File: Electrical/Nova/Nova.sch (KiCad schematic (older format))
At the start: 15 parts, among them J2 Conn_02x04_Counter_Clockwise, U1 STM32F411CEUx

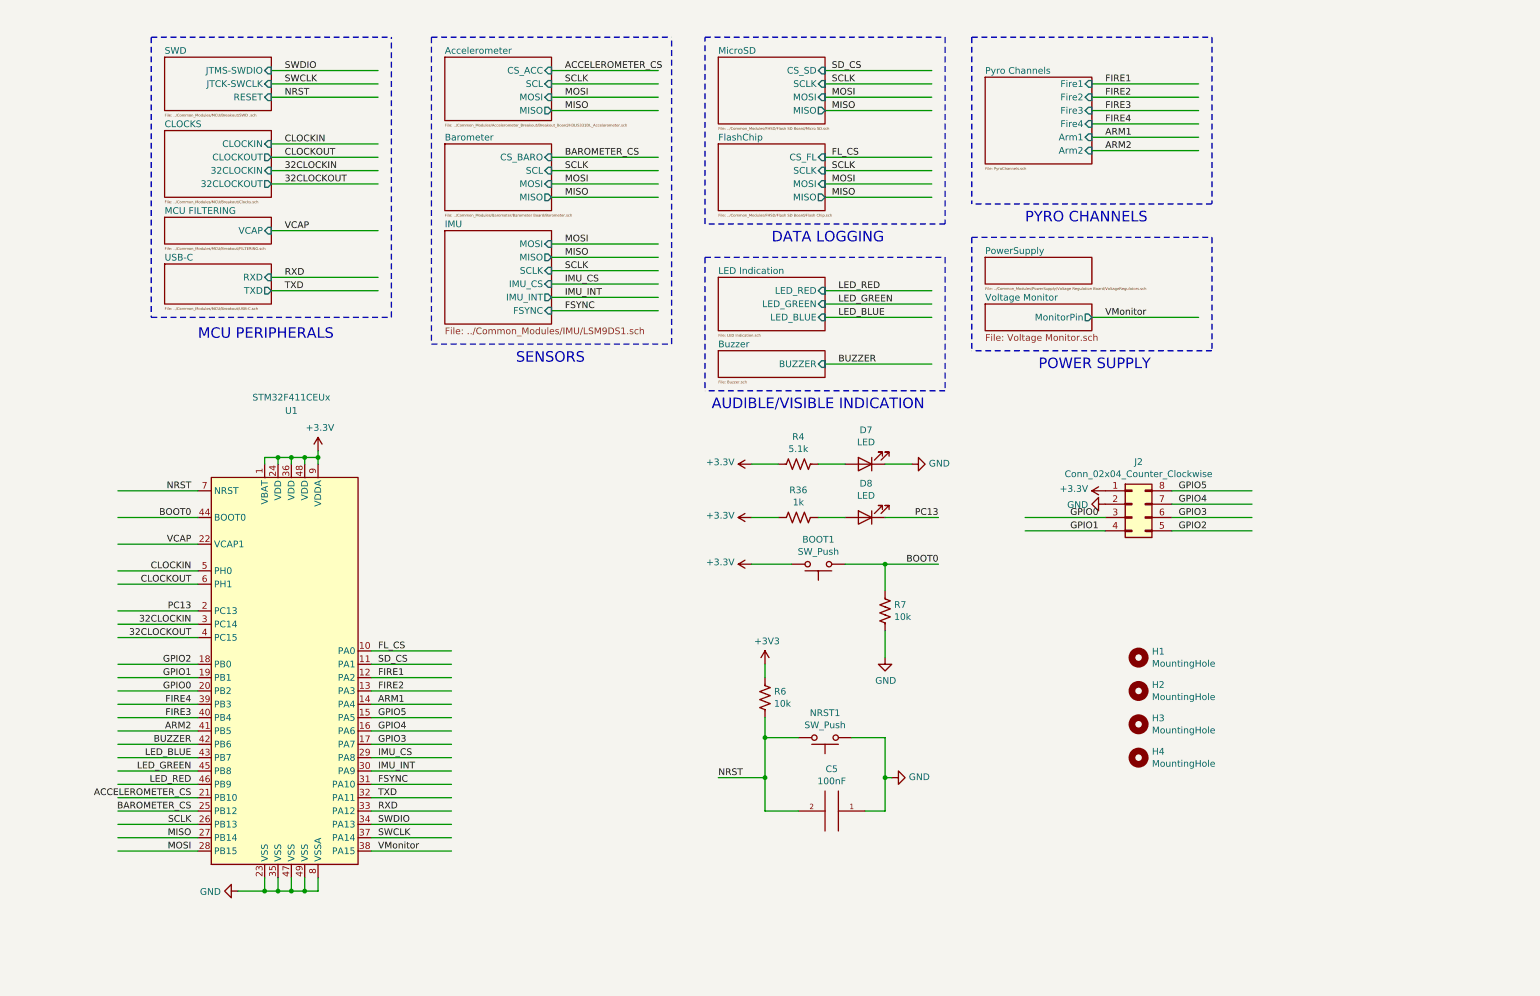
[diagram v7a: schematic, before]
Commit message: Flipped SD, fixed U8 pads, & put 2 INT pins on Accelerometer
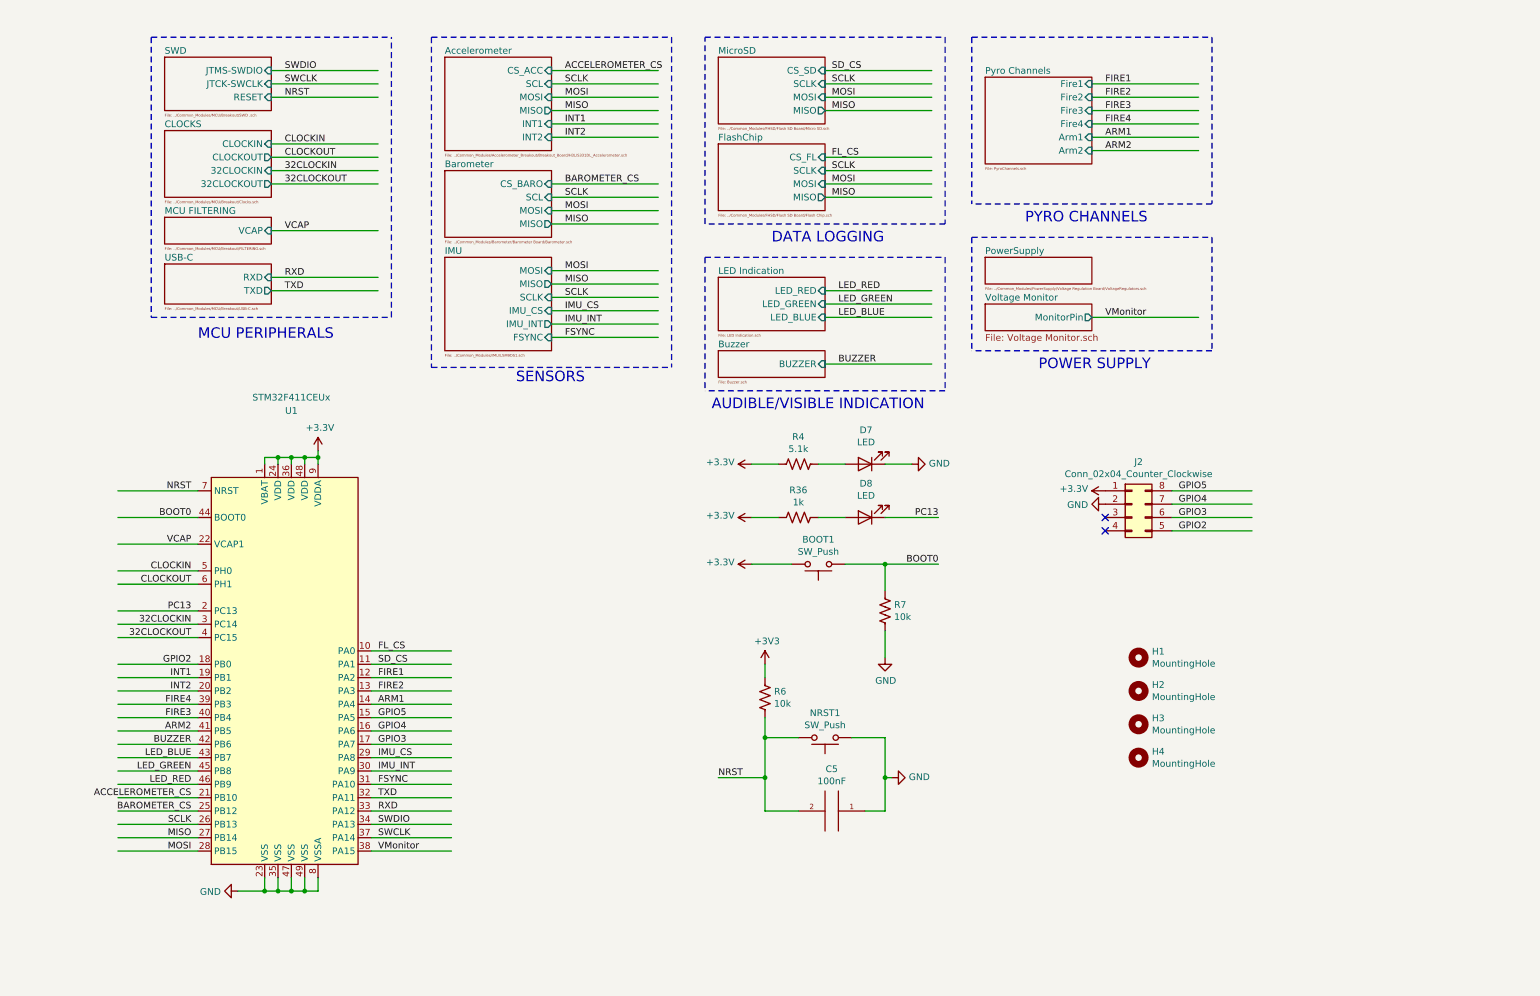
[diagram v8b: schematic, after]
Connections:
- net labels added: INT1, INT2
- net labels removed: GPIO0, GPIO1
- no-connect marks 0 -> 2
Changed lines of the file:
@@
 Wire Wire Line
 	6600 2850 7400 2850
-Text Notes 4800 3329 2    79   ~ 0
+Text Notes 4800 3475 2    79   ~ 0
 SENSORS\n\n
 Text Label 6650 1100 0    50   ~ 0
@@
 	5350 1100 4550 1100
 $Sheet
-S 3750 900  800  475
+S 3750 900  800  700
 U 5F46051D
 F0 "Accelerometer" 50
@@
 F4 "MISO" O R 4550 1300 50
 F5 "MOSI" I R 4550 1200 50
+F6 "INT1" I R 4550 1400 50
+F7 "INT2" I R 4550 1500 50
 $EndSheet
 Text Label 4650 1100 0    50   ~ 0
@@
 	5350 1200 4550 1200
 $Sheet
-S 3750 1550 800  500
+S 3750 1750 800  500
 U 5F3A063C
 F0 "Barometer" 50
 F1 "../Common_Modules/Barometer/Barometer Board/Barometer.sch" 20
-F2 "SCL" I R 4550 1750 50
-F3 "MOSI" I R 4550 1850 50
-F4 "MISO" O R 4550 1950 50
-F5 "CS_BARO" I R 4550 1650 50
+F2 "SCL" I R 4550 1950 50
+F3 "MOSI" I R 4550 2050 50
+F4 "MISO" O R 4550 2150 50
+F5 "CS_BARO" I R 4550 1850 50
 $EndSheet
-Text Label 4650 1750 0    50   ~ 0
+Text Label 4650 1950 0    50   ~ 0
 SCLK
-Text Label 4650 1950 0    50   ~ 0
+Text Label 4650 2150 0    50   ~ 0
 MISO
-Text Label 4650 1850 0    50   ~ 0
+Text Label 4650 2050 0    50   ~ 0
 MOSI
 Wire Wire Line
-	4550 1650 5350 1650
+	4550 1850 5350 1850
+Wire Wire Line
+	5350 2150 4550 2150
+Wire Wire Line
+	5350 2050 4550 2050
 Wire Wire Line
 	5350 1950 4550 1950
-Wire Wire Line
-	5350 1850 4550 1850
-Wire Wire Line
-	5350 1750 4550 1750
 Wire Wire Line
 	7400 1100 6600 1100
@@
 FL_CS
 Wire Notes Line
-	3650 3050 5450 3050
+	3650 3225 5450 3225
 Wire Notes Line
 	3650 750  5450 750
@@
 Text Label 3250 6650 0    50   ~ 0
 SWDIO
-Text Label 4650 1650 0    50   ~ 0
+Text Label 4650 1850 0    50   ~ 0
 BAROMETER_CS
 Text Label 4650 1000 0    50   ~ 0
@@
 	6150 5450 6150 5550
 $Sheet
-S 3750 2200 800  700
+S 3750 2400 800  700
 U 6029A10C
 F0 "IMU" 50
-F1 "../Common_Modules/IMU/LSM9DS1.sch" 50
-F2 "MOSI" I R 4550 2300 50
-F3 "MISO" O R 4550 2400 50
-F4 "SCLK" I R 4550 2500 50
-F5 "IMU_CS" I R 4550 2600 50
-F6 "IMU_INT" O R 4550 2700 50
-F7 "FSYNC" I R 4550 2800 50
+F1 "../Common_Modules/IMU/LSM9DS1.sch" 20
+F2 "MOSI" I R 4550 2500 50
+F3 "MISO" O R 4550 2600 50
+F4 "SCLK" I R 4550 2700 50
+F5 "IMU_CS" I R 4550 2800 50
+F6 "IMU_INT" O R 4550 2900 50
+F7 "FSYNC" I R 4550 3000 50
 $EndSheet
 Wire Wire Line
-	4550 2300 5350 2300
+	4550 2500 5350 2500
+Wire Wire Line
+	5350 2800 4550 2800
+Wire Wire Line
+	5350 2700 4550 2700
 Wire Wire Line
 	5350 2600 4550 2600
 Wire Wire Line
-	5350 2500 4550 2500
-Wire Wire Line
-	5350 2400 4550 2400
-Wire Wire Line
-	5350 2800 4550 2800
-Wire Wire Line
-	5350 2700 4550 2700
-Text Label 4650 2300 0    50   ~ 0
+	5350 3000 4550 3000
+Wire Wire Line
+	5350 2900 4550 2900
+Text Label 4650 2500 0    50   ~ 0
 MOSI
-Text Label 4650 2400 0    50   ~ 0
+Text Label 4650 2600 0    50   ~ 0
 MISO
-Text Label 4650 2500 0    50   ~ 0
+Text Label 4650 2700 0    50   ~ 0
 SCLK
-Text Label 4650 2600 0    50   ~ 0
+Text Label 4650 2800 0    50   ~ 0
 IMU_CS
-Text Label 4650 2700 0    50   ~ 0
+Text Label 4650 2900 0    50   ~ 0
 IMU_INT
-Text Label 4650 2800 0    50   ~ 0
+Text Label 4650 3000 0    50   ~ 0
 FSYNC
-Wire Notes Line
-	5450 3050 5450 750
-Wire Notes Line
-	3650 750  3650 3050
 Wire Wire Line
 	2500 3900 2400 3900
@@
 	9800 4350 9200 4350
 Wire Wire Line
-	8100 4350 8700 4350
-Wire Wire Line
-	8700 4450 8100 4450
-Wire Wire Line
 	9200 4450 9800 4450
-Text Label 8650 4350 2    50   ~ 0
-GPIO0
-Text Label 8650 4450 2    50   ~ 0
-GPIO1
 Text Label 9250 4450 0    50   ~ 0
 GPIO2
@@
 Wire Wire Line
 	1900 5450 1300 5450
-Text Label 1850 5650 2    50   ~ 0
-GPIO0
 Text Label 1850 5550 2    50   ~ 0
-GPIO1
+INT1
 Text Label 1850 5450 2    50   ~ 0
 GPIO2
@@
 Text Label 3250 5850 0    50   ~ 0
 GPIO5
+Wire Notes Line
+	3650 750  3650 3225
+Wire Notes Line
+	5450 750  5450 3225
+Wire Wire Line
+	4550 1400 5350 1400
+Wire Wire Line
+	4550 1500 5350 1500
+Text Label 4650 1400 0    50   ~ 0
+INT1
+Text Label 4650 1500 0    50   ~ 0
+INT2
+Text Label 1850 5650 2    50   ~ 0
+INT2
+NoConn ~ 8700 4350
+NoConn ~ 8700 4450
 $EndSCHEMATC
